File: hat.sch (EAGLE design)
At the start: 23 parts

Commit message: Version 3 ready for public
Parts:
- removed ADS1115: (no value), SparkFun-Connectors:M10SILK_FEMALE_PTH
- removed ADXL345: (no value), SparkFun-Connectors:M08SILK_FEMALE_PTH
- removed D3, D4: (no value), adafruit:SCHOTTKY-DIODEDO41-7
- removed D5, D6, D7: TVS, adafruit:DIODEDO-1N4148
- added C10: 0.1uF, microbuilder:CAP_CERAMIC0805
- added C11, C12: 22pF, microbuilder:CAP_CERAMIC0805
- added C4, C5, C9: 0.1µF, microbuilder:CAP_CERAMIC0805
- added C6: 10uF, SparkFun-Capacitors:CAP_POL1206
- added C7, C8: 560pF, microbuilder:CAP_CERAMIC0805
- added FRAME2: FRAME-LETTERNO_PACKAGE, SparkFun-Aesthetics:FRAME-LETTERNO_PACKAGE
- added J3: (no value), SparkFun-Connectors:M023.5MM
- added OK1: 4N35SM, optocoupler:4N35SM
- added R10: 10k, SparkFun-Passives:RESISTOR0805-RES
- added R11: 22k, SparkFun-Passives:RESISTOR0805-RES
- added R12, R7: 4k7, SparkFun-Passives:RESISTOR0805-RES
- added R8, R9: 100, SparkFun-Passives:RESISTOR0805-RES
- added U1: ADS1115IDGST, microbuilder:ADC_ADS1015
- added U2: ADXL345, SparkFun-Sensors:ADXL345
- added U3: MCP2515-I/SO, mcp2515:MCP2515-I/SO
- added U4: MCP2551, SparkFun-DigitalIC:MCP2551
- added VD1, VD2: (no value), diode:DIODE-SCHOTTKY-SOD523
- added X1: 16Mhz, IQD-Frequency-Products:CRYSTALS-NOGND-4-HSMX
- C1, C2: value 100uF -> 10uF; device SparkFun-Passives:CAP_POLPTH1 -> SparkFun-Capacitors:CAP_POL1206
- C3: value 100uF -> 1µF; device SparkFun-Passives:CAP_POLPTH1 -> microbuilder:CAP_CERAMIC0805
- D1: device adafruit:SCHOTTKY-DIODEDO41-7 -> diode:DIODE-DO214AC
- D2: device adafruit:SCHOTTKY-DIODEDO41-7 -> diode:DIODE-2CA|ACSOT23
- J1, J2: device SparkFun-Connectors:M025MM -> SparkFun-Connectors:M03SCREW
- R1, R2, R3, R4, R5: device SparkFun-Passives:RESISTORAXIAL-0.3 -> SparkFun-Passives:RESISTOR0805-RES
- R6: value 1k -> 10k; device SparkFun-Passives:RESISTORAXIAL-0.3 -> SparkFun-Passives:RESISTOR0805-RES
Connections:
- removed net 5.0V: RPI1.5.0V, RPI1.5.0V@1
- removed net A3: ADS1115.1
- removed net ALRT: ADS1115.5
- removed net BAT-LINKED: ADS1115.2, D7.C
- removed net INT1: ADXL345.4
- removed net INT2: ADXL345.5
- removed net N$1: D1.A, J1.1
- removed net N$10: C3.+, D7.A, R5.2, R6.2
- removed net N$2: D2.A, J1.2
- removed net N$5: D1.C, R1.1
- removed net N$7: D2.C, R3.1
- removed net N$9: D3.C, R5.1
- new net 5V: C9.P$1, RPI1.5.0V, RPI1.5.0V@1, U4.VSS
- new net BAT-1-INPUT: D2.K1, J1.2, R1.1
- new net BAT-2-INPUT: D2.K2, J1.3, R3.1
- new net CANH: J3.1, R8.2, U4.CANH
- new net CANL: J3.2, R9.2, U4.CANL
- new net LINKED-INPUT: J2.3, R5.1
- new net N$14: C12.P$1, U3.OSC1, X1.2
- new net N$15: C11.P$1, U3.OSC2, X1.1
- new net RS: R7.2, U4.RS
- new net RXCAN: R10.2, U4.RXD
- new net SHUNT-HIGH-INPUT: J2.1, U1.AIN2, VD1.C
- new net SHUNT-LOW-INPUT: J2.2, U1.AIN3, VD2.C
- new net TXCAN: U3.TXCAN, U4.TXD
- new net U5_RST: R12.1, U3.RESET
- new net VEHICLE-GND: D1.C, J1.1
- net 3.3V: now also C10.P$1, C3.P$2, C4.P$1, C5.P$1, C6.+, R12.2, U1.VDD, U2.CS, U2.SDO, U2.VDD, U2.VS, U3.VDD; no longer ADS1115.10, ADXL345.2, ADXL345.3, ADXL345.6
- net ADDR: now also R6.2, U1.ADDR; no longer ADS1115.6
- net BAT-1: now also C1.+, R1.2, R2.2, U1.AIN1; no longer ADS1115.4, D5.C
- net BAT-2: now also C2.+, R3.2, R4.2, U1.AIN0; no longer ADS1115.3, D6.C
- net GND: now also C10.P$2, C11.P$2, C12.P$2, C3.P$1, C4.P$2, C5.P$2, C6.-, C7.P$2, C8.P$2, C9.P$2, D1.A, D2.A, OK1.C, OK1.EMI, R11.1, R7.1, U1.GND, U2.GND@2, U2.GND@4, U2.GND@5, U3.VSS, U4.VDD, VD1.A, VD2.A; no longer ADS1115.9, ADXL345.1, C3.-, D4.A
- net GPIO25: now also U3.INT
- net GPIO5: now also OK1.COL
- net N$3: now also OK1.A, R5.2; no longer D3.A, J2.1
- net N$4: now also R10.1, R11.2, U3.RXCAN; no longer D4.C, J2.2
- net N$6: now also C7.P$1, R8.1; no longer C1.+, D5.A, R1.2, R2.2
- net N$8: now also C8.P$1, R9.1; no longer C2.+, D6.A, R3.2, R4.2
- net SCL: now also U1.SCL, U2.SCL; no longer ADS1115.8, ADXL345.8
- net SDA: now also U1.SDA, U2.SDA; no longer ADS1115.7, ADXL345.7
- net SPI_CE0: now also U3.CS
- net SPI_MISO: now also U3.SO
- net SPI_MOSI: now also U3.SI
- net SPI_SCLK: now also U3.SCK
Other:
- note added: "Default I²C Address = 1001000"
- note added: "Note: Internal pull-up"
- note added: "v3"
- note removed: "v1"

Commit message: Cleanup text
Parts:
- FRAME1: value FRAME-LETTER -> FRAME-LETTERNO_PACKAGE; device SparkFun-Aesthetics:FRAME-LETTER -> SparkFun-Aesthetics:FRAME-LETTERNO_PACKAGE
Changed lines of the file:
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@@
 <part name="GND1" library="supply1" deviceset="GND" device=""/>
 <part name="GND2" library="supply1" deviceset="GND" device=""/>
-<part name="FRAME1" library="SparkFun-Aesthetics" deviceset="FRAME-LETTER" device=""/>
+<part name="FRAME1" library="SparkFun-Aesthetics" deviceset="FRAME-LETTER" device="NO_PACKAGE" value="FRAME-LETTERNO_PACKAGE"/>
 <part name="GND3" library="SparkFun-Aesthetics" deviceset="GND" device=""/>
 <part name="GND4" library="SparkFun-Aesthetics" deviceset="GND" device=""/>

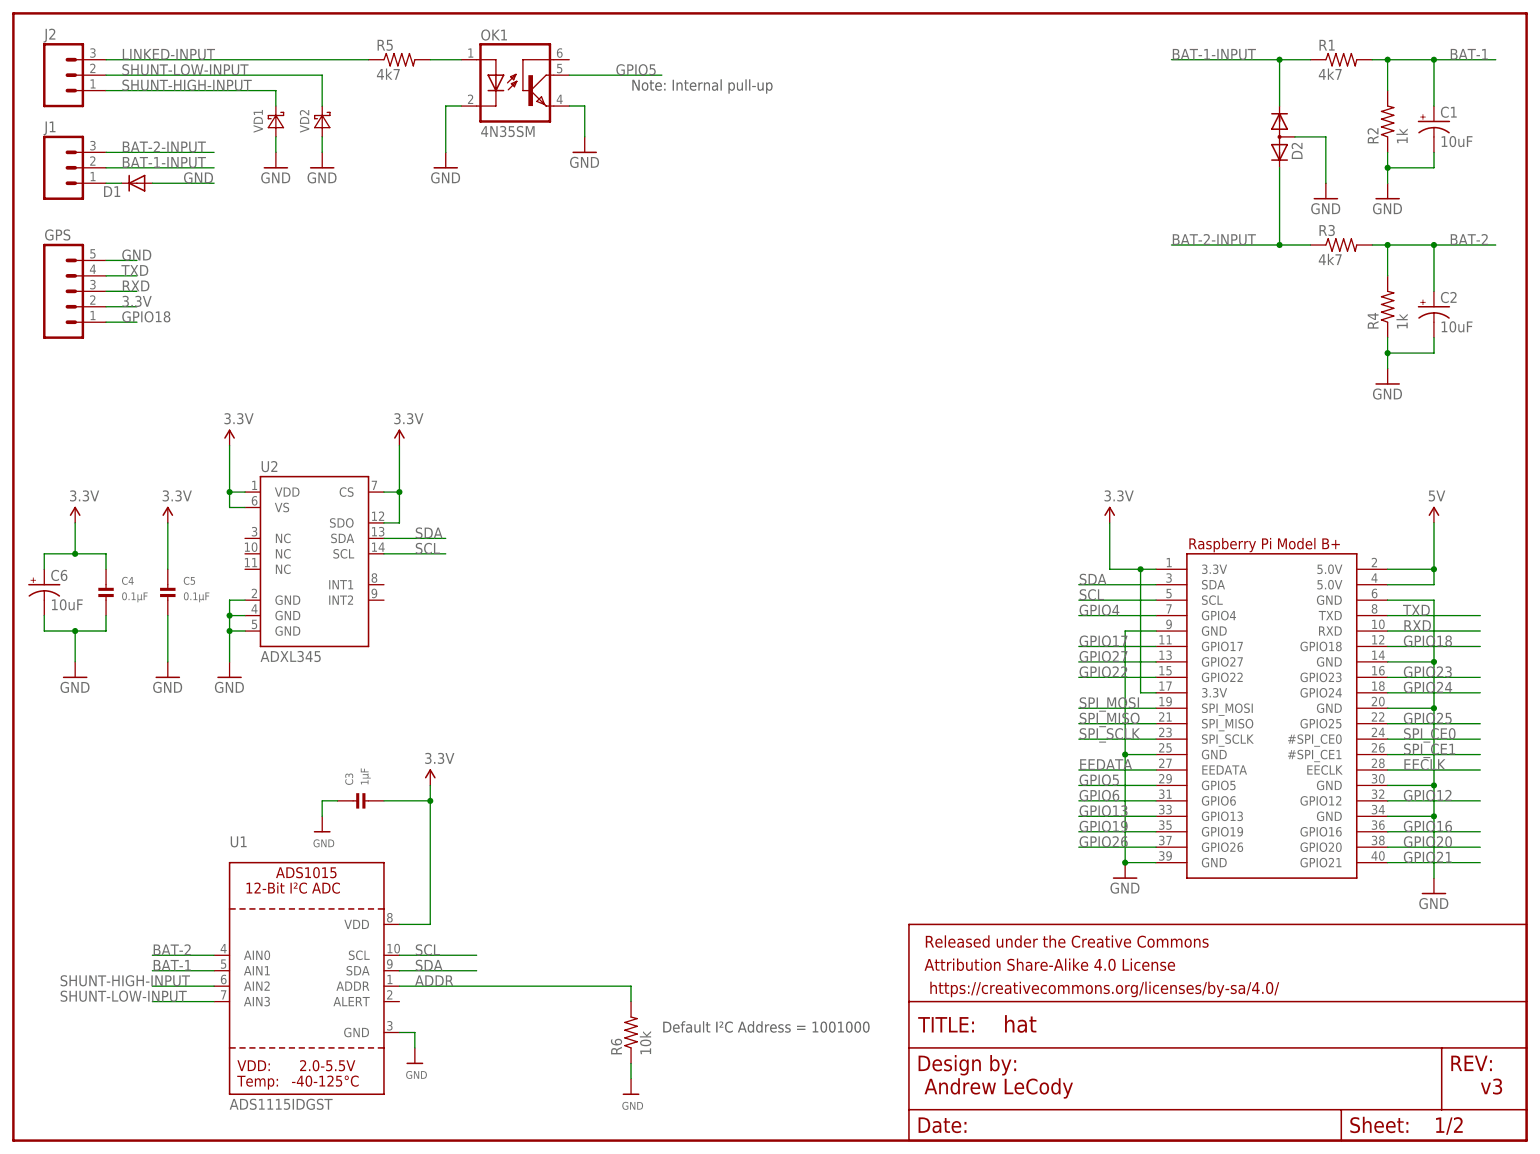
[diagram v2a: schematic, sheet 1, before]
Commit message: Added 1kOhm resistors on inputs
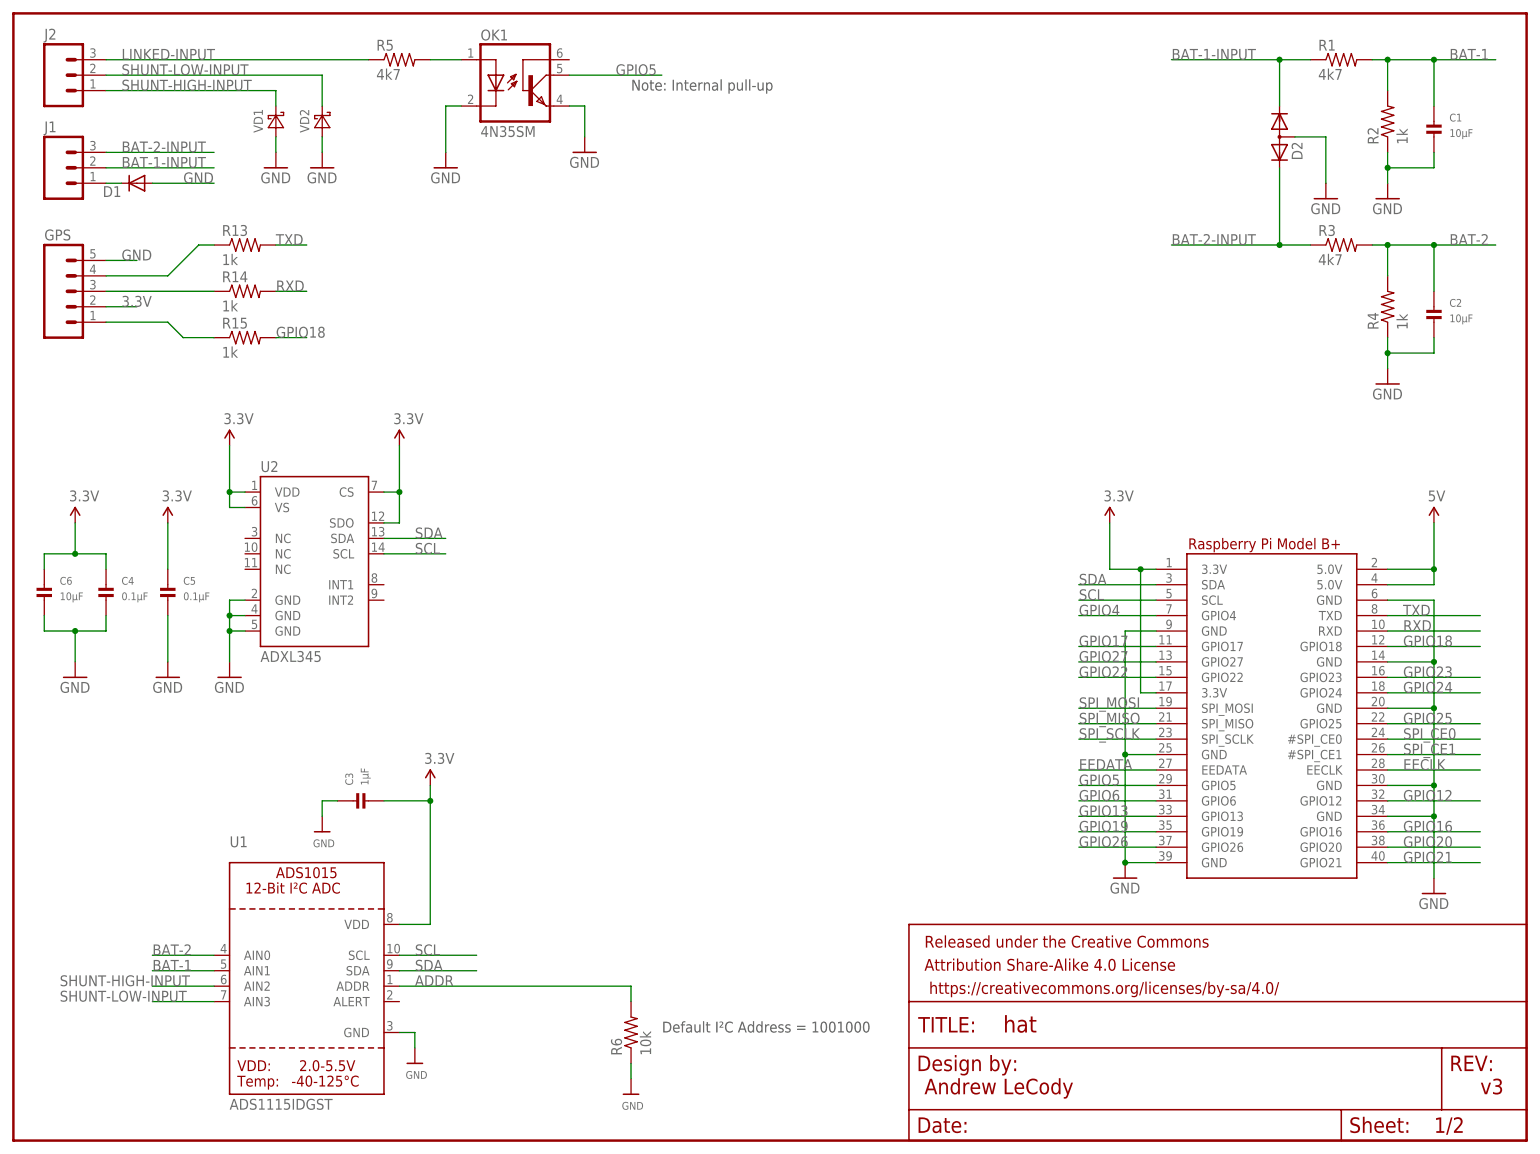
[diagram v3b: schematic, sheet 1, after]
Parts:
- added R13, R14, R15: 1k, SparkFun-Passives:RESISTOR0805-RES
- C1, C2, C6: value 10uF -> 10µF; device SparkFun-Capacitors:CAP_POL1206 -> microbuilder:CAP_CERAMIC0805
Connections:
- new net N$1: GPS.4, R13.1
- new net N$2: GPS.3, R14.1
- new net N$5: GPS.1, R15.1
- net 3.3V: now also C6.P$1; no longer C6.+
- net BAT-1: now also C1.P$1; no longer C1.+
- net BAT-2: now also C2.P$1; no longer C2.+
- net GND: now also C1.P$2, C2.P$2, C6.P$2; no longer C1.-, C2.-, C6.-
- net GPIO18: now also R15.2; no longer GPS.1
- net RXD: now also R14.2; no longer GPS.3
- net TXD: now also R13.2; no longer GPS.4
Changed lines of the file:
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@@
 <part name="GND12" library="SparkFun" deviceset="GND" device=""/>
 <part name="GND13" library="SparkFun" deviceset="GND" device=""/>
-<part name="C6" library="SparkFun-Capacitors" deviceset="CAP_POL" device="1206" value="10uF"/>
 <part name="U1" library="microbuilder" deviceset="ADC_ADS1015" device="" value="ADS1115IDGST"/>
 <part name="C3" library="microbuilder" deviceset="CAP_CERAMIC" device="0805" value="1µF"/>
@@
 <part name="C4" library="microbuilder" deviceset="CAP_CERAMIC" device="0805" value="0.1µF"/>
 <part name="C5" library="microbuilder" deviceset="CAP_CERAMIC" device="0805" value="0.1µF"/>
-<part name="C2" library="SparkFun-Capacitors" deviceset="CAP_POL" device="1206" value="10uF"/>
 <part name="R5" library="SparkFun-Passives" deviceset="RESISTOR" device="0805-RES" value="4k7"/>
 <part name="R1" library="SparkFun-Passives" deviceset="RESISTOR" device="0805-RES" value="4k7"/>
 <part name="R2" library="SparkFun-Passives" deviceset="RESISTOR" device="0805-RES" value="1k"/>
-<part name="C1" library="SparkFun-Capacitors" deviceset="CAP_POL" device="1206" value="10uF"/>
 <part name="R3" library="SparkFun-Passives" deviceset="RESISTOR" device="0805-RES" value="4k7"/>
 <part name="R4" library="SparkFun-Passives" deviceset="RESISTOR" device="0805-RES" value="1k"/>
@@
 <part name="J2" library="SparkFun-Connectors" deviceset="M03" device="SCREW"/>
 <part name="J3" library="SparkFun-Connectors" deviceset="M02" device="3.5MM"/>
+<part name="C6" library="microbuilder" deviceset="CAP_CERAMIC" device="0805" value="10µF"/>
+<part name="C1" library="microbuilder" deviceset="CAP_CERAMIC" device="0805" value="10µF"/>
+<part name="C2" library="microbuilder" deviceset="CAP_CERAMIC" device="0805" value="10µF"/>
+<part name="R13" library="SparkFun-Passives" deviceset="RESISTOR" device="0805-RES" value="1k"/>
+<part name="R14" library="SparkFun-Passives" deviceset="RESISTOR" device="0805-RES" value="1k"/>
+<part name="R15" library="SparkFun-Passives" deviceset="RESISTOR" device="0805-RES" value="1k"/>
 </parts>
 <sheets>
@@
 <instance part="GND12" gate="1" x="10.16" y="76.2"/>
 <instance part="GND13" gate="1" x="25.4" y="76.2"/>
-<instance part="C6" gate="G$1" x="5.08" y="91.44"/>
 <instance part="U1" gate="G$1" x="48.26" y="27.94"/>
 <instance part="C3" gate="G$1" x="58.42" y="55.88" rot="R90"/>
@@
 <instance part="C4" gate="G$1" x="15.24" y="88.9"/>
 <instance part="C5" gate="G$1" x="25.4" y="88.9"/>
-<instance part="C2" gate="G$1" x="233.68" y="137.16"/>
 <instance part="R5" gate="G$1" x="63.5" y="177.8"/>
 <instance part="R1" gate="G$1" x="218.44" y="177.8"/>
 <instance part="R2" gate="G$1" x="226.06" y="167.64" rot="R90"/>
-<instance part="C1" gate="G$1" x="233.68" y="167.64"/>
 <instance part="R3" gate="G$1" x="218.44" y="147.32"/>
 <instance part="R4" gate="G$1" x="226.06" y="137.16" rot="R90"/>
@@
 <instance part="J1" gate="J$1" x="7.62" y="160.02"/>
 <instance part="J2" gate="J$1" x="7.62" y="175.26"/>
+<instance part="C6" gate="G$1" x="5.08" y="88.9"/>
+<instance part="C1" gate="G$1" x="233.68" y="165.1"/>
+<instance part="C2" gate="G$1" x="233.68" y="134.62"/>
+<instance part="R13" gate="G$1" x="38.1" y="147.32"/>
+<instance part="R14" gate="G$1" x="38.1" y="139.7"/>
+<instance part="R15" gate="G$1" x="38.1" y="132.08"/>
 </instances>
 <busses>
@@
 <wire x1="15.24" y1="96.52" x2="10.16" y2="96.52" width="0.1524" layer="91"/>
 <junction x="10.16" y="96.52"/>
-<pinref part="C6" gate="G$1" pin="+"/>
 <pinref part="SUPPLY2" gate="G$1" pin="3.3V"/>
 <pinref part="C4" gate="G$1" pin="P$1"/>
+<pinref part="C6" gate="G$1" pin="P$1"/>
 </segment>
 <segment>
@@
 <junction x="226.06" y="160.02"/>
 <pinref part="R2" gate="G$1" pin="1"/>
-<pinref part="C1" gate="G$1" pin="-"/>
+<pinref part="C1" gate="G$1" pin="P$2"/>
 </segment>
 <segment>
@@
 <junction x="226.06" y="129.54"/>
 <pinref part="GND4" gate="1" pin="GND"/>
-<pinref part="C2" gate="G$1" pin="-"/>
 <pinref part="R4" gate="G$1" pin="1"/>
+<pinref part="C2" gate="G$1" pin="P$2"/>
 </segment>
 <segment>
@@
 <wire x1="15.24" y1="83.82" x2="10.16" y2="83.82" width="0.1524" layer="91"/>
 <junction x="10.16" y="83.82"/>
-<pinref part="C6" gate="G$1" pin="-"/>
 <pinref part="GND12" gate="1" pin="GND"/>
 <pinref part="C4" gate="G$1" pin="P$2"/>
+<pinref part="C6" gate="G$1" pin="P$2"/>
 </segment>
 <segment>
@@
 </segment>
 <segment>
-<pinref part="GPS" gate="G$1" pin="4"/>
-<wire x1="15.24" y1="142.24" x2="20.32" y2="142.24" width="0.1524" layer="91"/>
-<label x="17.78" y="142.24" size="1.778" layer="95"/>
+<pinref part="R13" gate="G$1" pin="2"/>
+<wire x1="43.18" y1="147.32" x2="48.26" y2="147.32" width="0.1524" layer="91"/>
+<label x="43.18" y="147.32" size="1.778" layer="95"/>
 </segment>
 </net>
@@
 </segment>
 <segment>
-<pinref part="GPS" gate="G$1" pin="3"/>
-<wire x1="15.24" y1="139.7" x2="20.32" y2="139.7" width="0.1524" layer="91"/>
-<label x="17.78" y="139.7" size="1.778" layer="95"/>
+<pinref part="R14" gate="G$1" pin="2"/>
+<wire x1="43.18" y1="139.7" x2="48.26" y2="139.7" width="0.1524" layer="91"/>
+<label x="43.18" y="139.7" size="1.778" layer="95"/>
 </segment>
 </net>
@@
 </segment>
 <segment>
-<pinref part="GPS" gate="G$1" pin="1"/>
-<wire x1="15.24" y1="134.62" x2="20.32" y2="134.62" width="0.1524" layer="91"/>
-<label x="17.78" y="134.62" size="1.778" layer="95"/>
+<pinref part="R15" gate="G$1" pin="2"/>
+<wire x1="43.18" y1="132.08" x2="48.26" y2="132.08" width="0.1524" layer="91"/>
+<label x="43.18" y="132.08" size="1.778" layer="95"/>
 </segment>
 </net>
@@
 <pinref part="R1" gate="G$1" pin="2"/>
 <pinref part="R2" gate="G$1" pin="2"/>
-<pinref part="C1" gate="G$1" pin="+"/>
+<pinref part="C1" gate="G$1" pin="P$1"/>
 </segment>
 <segment>
@@
 <junction x="226.06" y="147.32"/>
 <junction x="233.68" y="147.32"/>
-<pinref part="C2" gate="G$1" pin="+"/>
 <pinref part="R3" gate="G$1" pin="2"/>
 <pinref part="R4" gate="G$1" pin="2"/>
+<pinref part="C2" gate="G$1" pin="P$1"/>
 </segment>
 <segment>
@@
 </segment>
 </net>
+<net name="N$1" class="0">
+<segment>
+<pinref part="GPS" gate="G$1" pin="4"/>
+<wire x1="15.24" y1="142.24" x2="25.4" y2="142.24" width="0.1524" layer="91"/>
+<wire x1="25.4" y1="142.24" x2="30.48" y2="147.32" width="0.1524" layer="91"/>
+<pinref part="R13" gate="G$1" pin="1"/>
+<wire x1="30.48" y1="147.32" x2="33.02" y2="147.32" width="0.1524" layer="91"/>
+</segment>
+</net>
+<net name="N$2" class="0">
+<segment>
+<pinref part="GPS" gate="G$1" pin="3"/>
+<pinref part="R14" gate="G$1" pin="1"/>
+<wire x1="15.24" y1="139.7" x2="33.02" y2="139.7" width="0.1524" layer="91"/>
+</segment>
+</net>
+<net name="N$5" class="0">
+<segment>
+<pinref part="GPS" gate="G$1" pin="1"/>
+<wire x1="15.24" y1="134.62" x2="25.4" y2="134.62" width="0.1524" layer="91"/>
+<wire x1="25.4" y1="134.62" x2="27.94" y2="132.08" width="0.1524" layer="91"/>
+<pinref part="R15" gate="G$1" pin="1"/>
+<wire x1="27.94" y1="132.08" x2="33.02" y2="132.08" width="0.1524" layer="91"/>
+</segment>
+</net>
